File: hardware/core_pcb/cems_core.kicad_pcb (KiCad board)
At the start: 4 copper layers, 211.5 x 85.1 mm, 423 parts, among them J1 24VDC IN, J10 BANK A IDC26, J11 BANK B, J12 INPUTS IDC26, J13 FIELD A 24V, J14 FIELD B 24V, J15 PUMP POWER, J16 PUMP SIGNALS, J17 RELAY COILS, J18 USB-C, J19 TEMP1, J2 CLIENT, J20 TEMP2, J21 TEMP3, J22 AI 1-2, J23 AI 3-4, J24 AI 5-6, J25 SENSORS, J3 I/O ONLY, J4 RVT70 RiBUS, J5 SWD, J6 SERVICE UART, J7 ROLE, Q1 2N7002, Q2 BC817, Q3 BC807, Q4 2N7002, Q5 BC817, Q6 BC807, SW1 RESET, U1 TPS54360B, U10 APS6404L, U11 MAX6369, U12 74LVC1G08, U13 74LVC1G04, U14 ISO2H823V2.5, U15 ISO808A-1, U16 ISO1I813T, U17 L78L05, U18 ISO7741, U19 74LVC1G08, U2 TLV62569DBV, U20 74LVC1G08, U21 IPS7091S, U22 74LVC1G14, U23 74LVC1G14, U24 LMV331, U25 CPC1017N, U26 CPC1017N, U27 USBLC6-2SC6, U28 ISOW7741, U29 74LVC1G04, U3 STM32H573VIT6, U30 ADS124S08, U31 ISOW7741, U32 74LVC1G04, U33 ITX2424SA, U34 AD4112, U35 L78L05, U36 LM317L, U37 REF5010, U38 LT3045, U4 LAN8742A-CZ, U5 TPD4E05U06, U6 W5500, U7 TPD4E05U06, U8 W25Q128JV, U9 MB85RC1MT, Y1 25MHz, Y2 32.768kHz, Y3 25MHz, Y4 25MHz

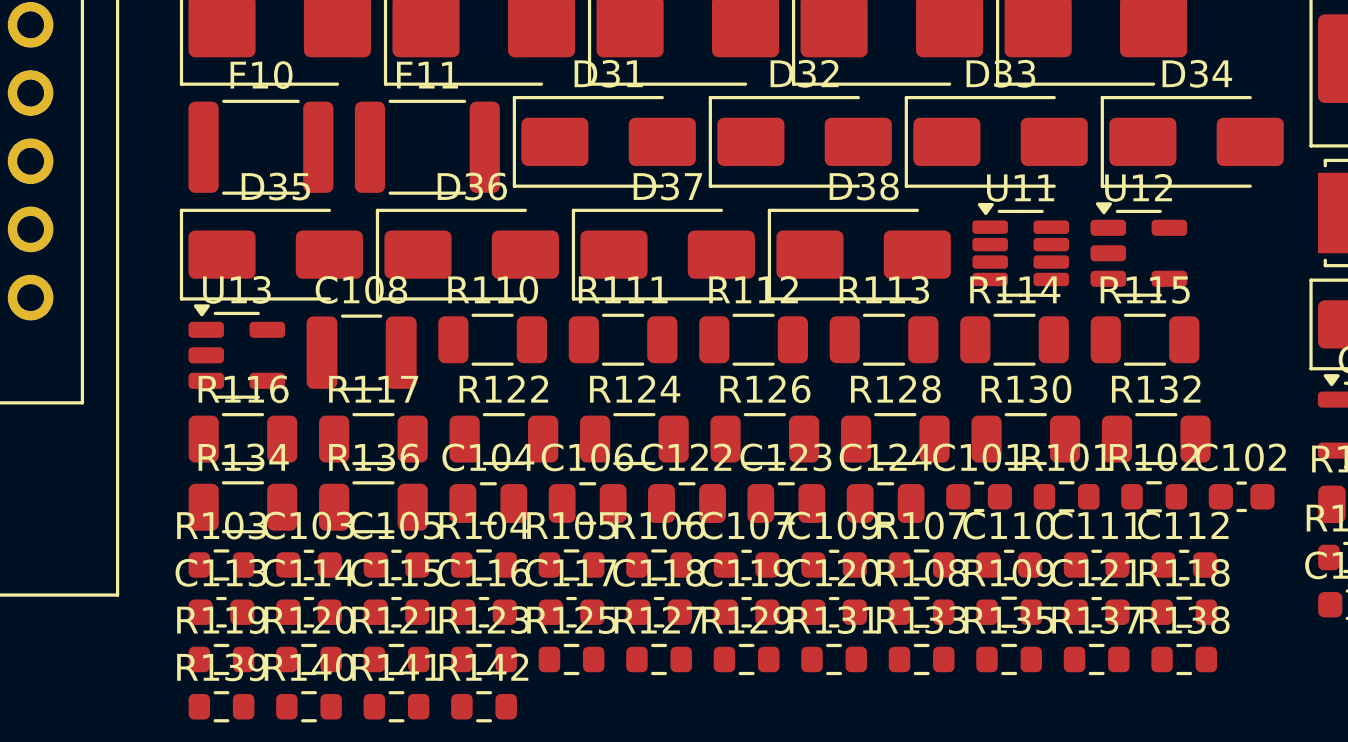
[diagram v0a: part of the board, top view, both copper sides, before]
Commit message: CORE PCB: I/O chip pinouts checked against datasheets; gate latch, ODIS polarity
Pin tables of AD4112, ADS124S08, ISO2H823V2.5, ISO1I813T, ISO808A-1, ISO7741 and
ISOW7741 compared with the datasheets: all match. Fixes from the check: ISO2H823 /ODIS
is active low (takes GATE directly); OLADJ fitted 12.1k; CLKADJ 10k 0.1 %; ROSC 22.1k;
ISOW7741 EN/FLT pulled to 3.3 V; MAX6369 WDO only pulses, so a 74LVC1G175 latches a
trip until GATE_EN is re-armed. hardware/datasheets/IO_CHIPS_DATASHEET_CHECK.md holds the
extracts and the AD4112 register facts for the driver.

Co-Authored-By: Claude Opus 5.5 <noreply@anthropic.com>
Claude-Session: https://claude.ai/code/session_014onnq3eRiDkqdAB6fKiRDW
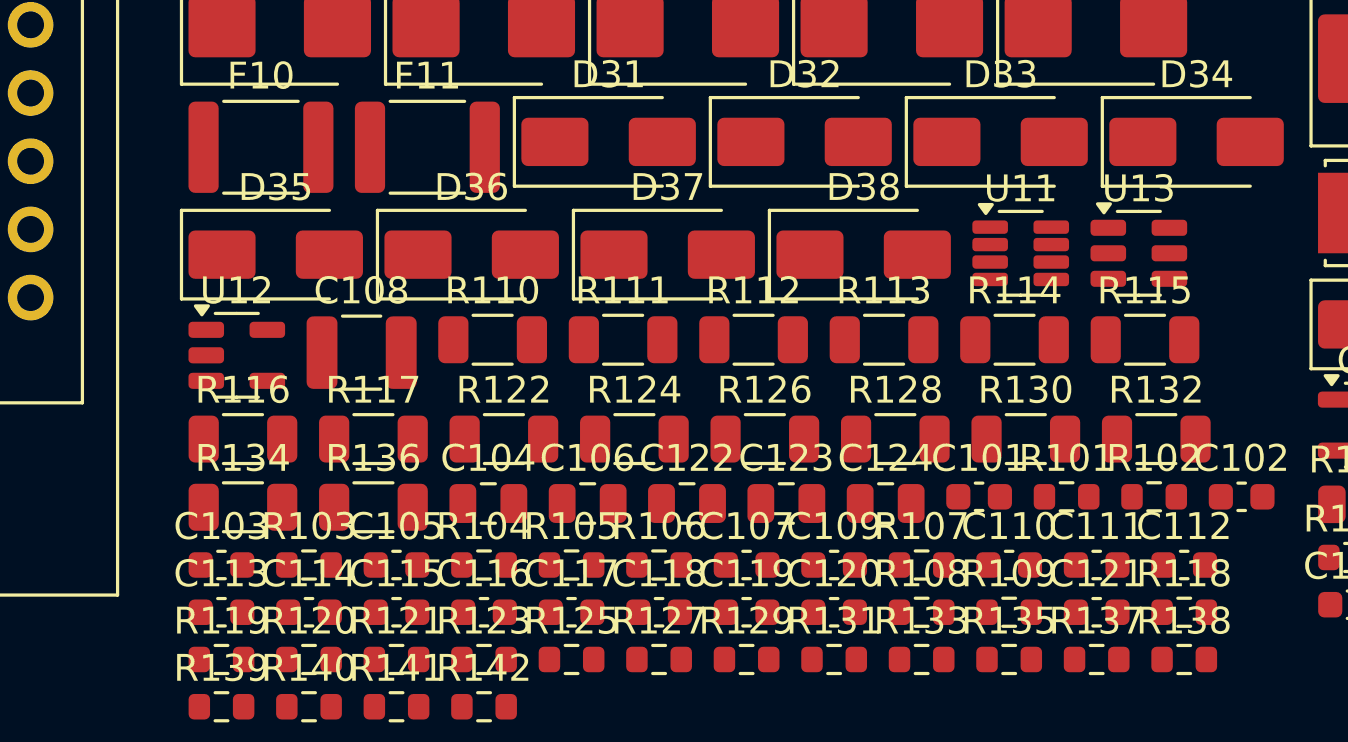
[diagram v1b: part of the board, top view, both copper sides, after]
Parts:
- R104: value 10k -> 10k 0.1%
- R106: value DNF -> 12k1 1%
- R118: value 22k 1% -> 22k1 1%
- U13: value 74LVC1G04 -> 74LVC1G175; footprint Package_TO_SOT_SMD:SOT-23-5 -> Package_TO_SOT_SMD:SOT-23-6
- moved U12 33.8 mm to (198.0, 156.1)
- moved U13 33.8 mm to (231.6, 152.3)
- moved C103 3.26 mm to (197.4, 163.9)
- moved R103 3.26 mm to (200.7, 163.9)
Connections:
- R164 pad 1: +5V -> +3V3
- R176 pad 1: +5V -> +3V3
- U12 pad 2: WDO_N -> GATE_ARM
- U13 pad 1: (no net) -> GATE_EN
- U13 pad 2: GATE -> GND
- U13 pad 3: GND -> +3V3
- U13 pad 4: GATE_N -> GATE_ARM
- U14 pad 40: GATE_N -> GATE

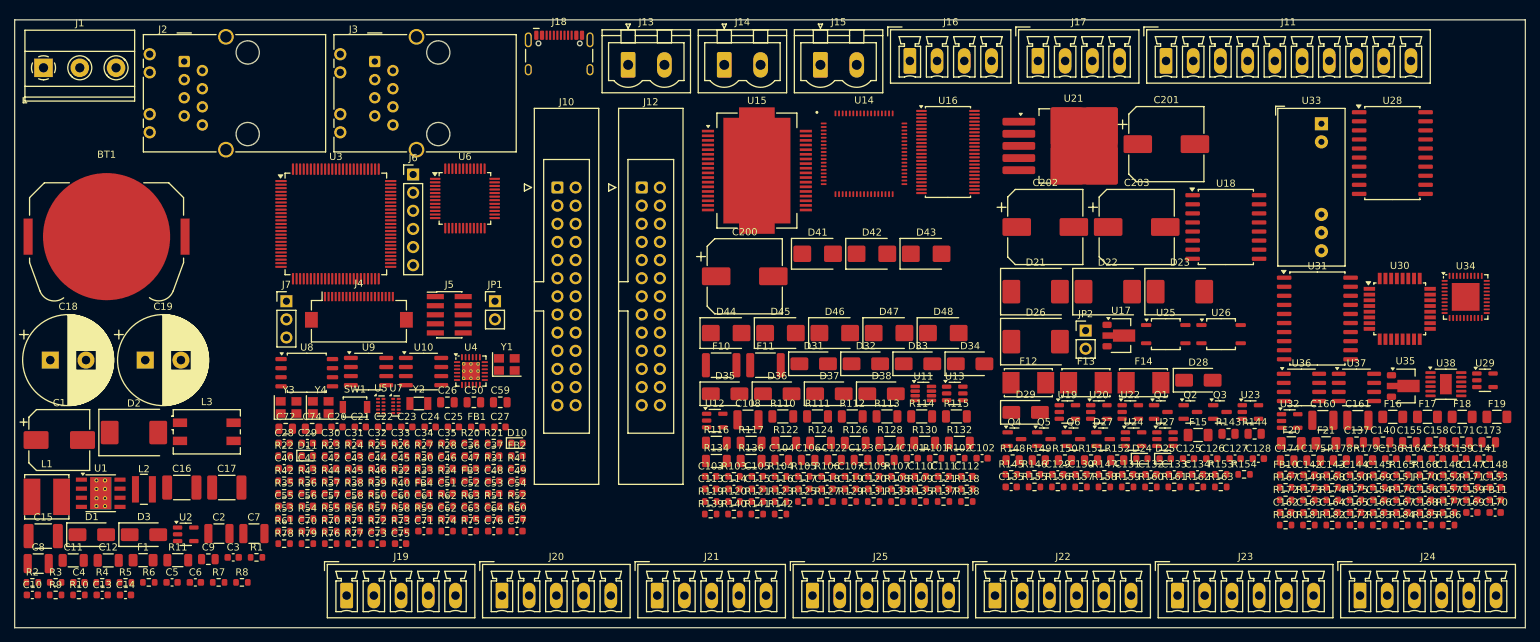
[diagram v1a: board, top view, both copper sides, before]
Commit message: One 40-way ribbon for all digital I/O (Gary, 31 Oct)
Main board: J10 becomes a 40-way latched IDC header carrying bank A outputs 1-8 (pins
1-16, each beside its 0 V) and inputs 1-8 (pins 17-32), with 4 x +24 V and 4 x 0 V; J12
and F11 removed, so no ribbon can go into the wrong slot. Breakout rev 0.2: one board,
50 x 80 mm, two-tier 3.81 mm pluggable headers (valves OUT over 0V, inputs IN over +24V,
plus a 0V strip for 3-wire sensors), LEDs on every channel, flyback options on the valves.
Two-tier footprint is a placeholder until the maker's drawing is checked.

Co-Authored-By: Claude Opus 5.5 <noreply@anthropic.com>
Claude-Session: https://claude.ai/code/session_014onnq3eRiDkqdAB6fKiRDW
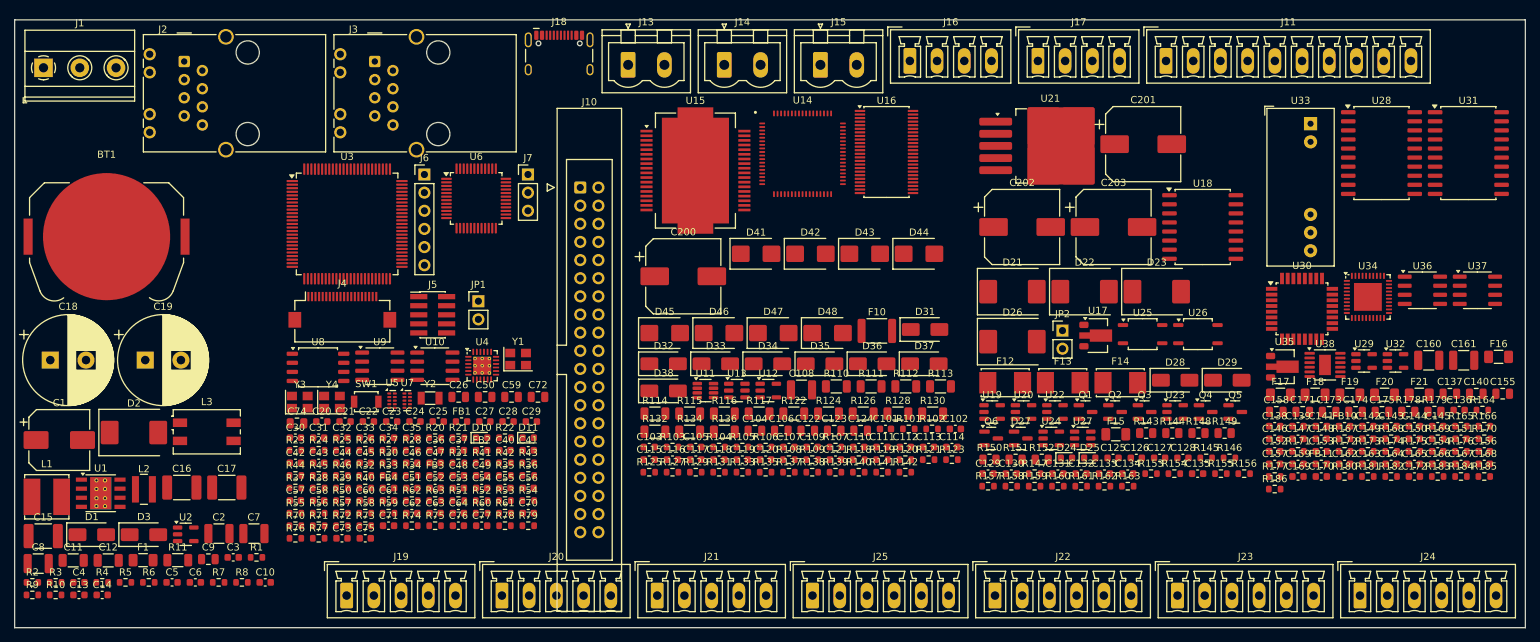
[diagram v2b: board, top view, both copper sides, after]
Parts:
- removed F11: 0.75A, Fuse:Fuse_1812_4532Metric
- removed J12: INPUTS IDC26, Connector_IDC:IDC-Header_2x13_P2.54mm_Latch_Vertical
- J10: value BANK A IDC26 -> DIGITAL I/O IDC40; footprint Connector_IDC:IDC-Header_2x13_P2.54mm_Latch_Vertical -> Connector_IDC:IDC-Header_2x20_P2.54mm_Latch_Vertical
- moved R132 42.7 mm to (189.6, 157.7)
- moved J7 38.2 mm to (171.9, 121.6)
- moved R114 37.3 mm to (189.6, 155.1)
- moved R115 37.3 mm to (194.5, 155.1)
- moved C72 35.6 mm to (173.3, 152.8)
- moved C10 32.6 mm to (135.1, 178.8)
- moved C28 31.5 mm to (169.1, 156.2)
- moved C29 31.5 mm to (172.3, 156.2)
- moved U31 31.4 mm to (303.5, 118.6)
- moved C113 31.1 mm to (228.0, 159.8)
- moved C114 31.1 mm to (231.2, 159.8)
- moved R78 31.0 mm to (168.6, 170.8)
- moved R79 31.0 mm to (171.9, 170.8)
- moved C40 31.0 mm to (168.6, 160.3)
- moved C41 31.0 mm to (171.9, 160.3)
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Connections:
- F10 pad 2: +24V_RA -> +24V_RIB
- J10 pad 17: +24V_RA -> DI1
- J10 pad 19: +24V_RA -> DI2
- J10 pad 21: +24V_RA -> DI3
- J10 pad 23: +24V_RA -> DI4
- J10 pad 25: +24V_RA -> DI5

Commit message: CORE PCB + breakout: make every user plug fit only its own header
Three pitch families (5.08 power/24 V outputs, 3.81 bank B, 3.5 sensors), one size per
header except the harmless temperature and 4-20 mA groups, and a coding key per header
(script-checked against every plug and shift). J13+J14 merged into one 4-way field plug;
pump power and signals on one 6-way plug (J16 gone); relays 3-way. Survival layer: 1k 1 W
pump outputs, per-channel relay PTCs + CPC1014N, 30 mA loop current limiters, TVS on the
5 V and 10 V sensor supplies. CORE_PCB.md section 15 has the mis-plug tables.

Co-Authored-By: Claude Opus 5.5 <noreply@anthropic.com>
Claude-Session: https://claude.ai/code/session_014onnq3eRiDkqdAB6fKiRDW
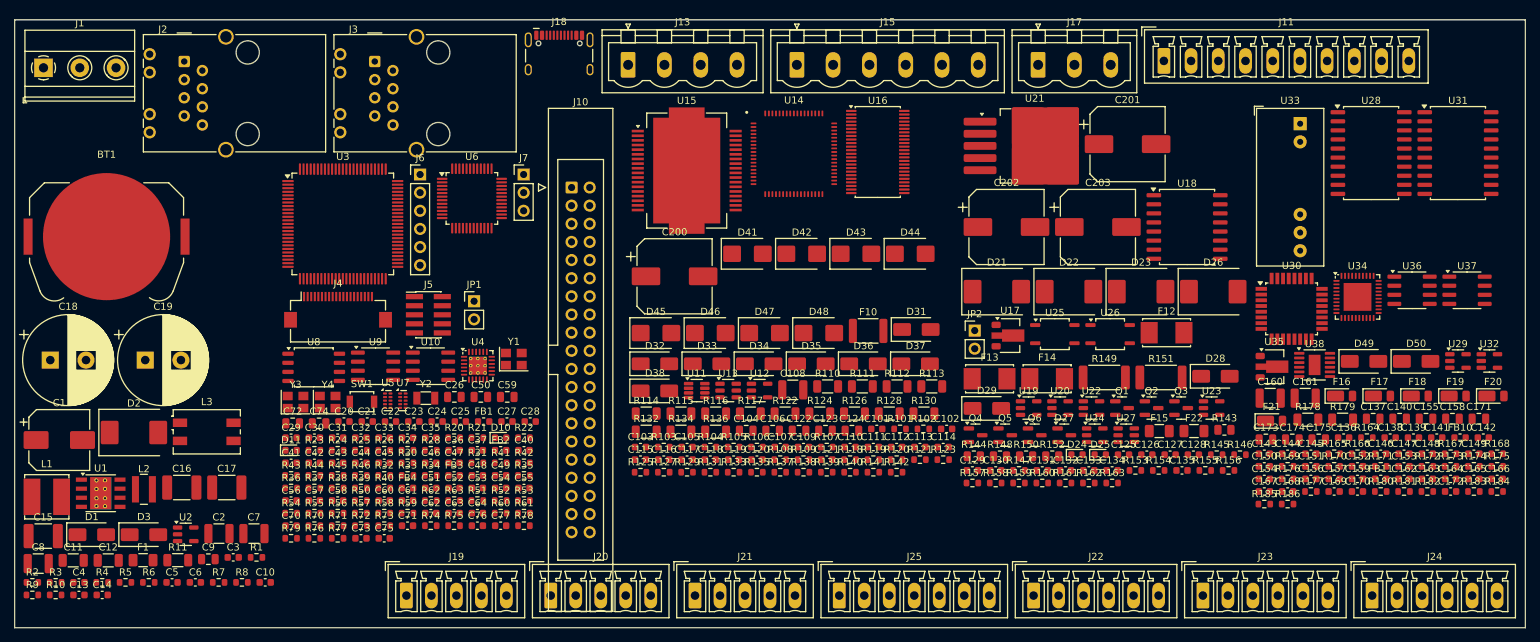
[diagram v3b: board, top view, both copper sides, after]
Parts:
- removed J14: FIELD B 24V, Connector_Phoenix_MSTB:PhoenixContact_MSTBVA_2,5_2-G-5,08_1x02_P5.08mm_Vertical
- removed J16: PUMP SIGNALS, Connector_Phoenix_MC:PhoenixContact_MCV_1,5_4-G-3.81_1x04_P3.81mm_Vertical
- added D49: SMAJ5.0A, Diode_SMD:D_SMA, F.Cu at (288.9, 147.8)
- added D50: SMAJ11A, Diode_SMD:D_SMA, F.Cu at (296.2, 147.8)
- added F22: 50mA, Fuse:Fuse_1206_3216Metric, F.Cu at (265.1, 157.6)
- F15: value 0.2A -> 50mA
- F16, F17, F18, F19, F20, F21: value 50mA -> CCR 30mA; footprint Fuse:Fuse_1206_3216Metric -> Diode_SMD:D_PowerDI-123
- J13: value FIELD A 24V -> FIELD 24V A+B; footprint Connector_Phoenix_MSTB:PhoenixContact_MSTBVA_2,5_2-G-5,08_1x02_P5.08mm_Vertical -> Connector_Phoenix_MSTB:PhoenixContact_MSTBVA_2,5_4-G-5,08_1x04_P5.08mm_Vertical
- J15: value PUMP POWER -> PUMP; footprint Connector_Phoenix_MSTB:PhoenixContact_MSTBVA_2,5_2-G-5,08_1x02_P5.08mm_Vertical -> Connector_Phoenix_MSTB:PhoenixContact_MSTBVA_2,5_6-G-5,08_1x06_P5.08mm_Vertical
- J17: footprint Connector_Phoenix_MC:PhoenixContact_MCV_1,5_4-G-3.81_1x04_P3.81mm_Vertical -> Connector_Phoenix_MSTB:PhoenixContact_MSTBVA_2,5_3-G-5,08_1x03_P5.08mm_Vertical
- J19, J20, J21: footprint Connector_Phoenix_MC:PhoenixContact_MCV_1,5_5-G-3.81_1x05_P3.81mm_Vertical -> Connector_Phoenix_MC:PhoenixContact_MCV_1,5_5-G-3.5_1x05_P3.50mm_Vertical
- J22, J23, J24: footprint Connector_Phoenix_MC:PhoenixContact_MCV_1,5_6-G-3.81_1x06_P3.81mm_Vertical -> Connector_Phoenix_MC:PhoenixContact_MCV_1,5_6-G-3.5_1x06_P3.50mm_Vertical
- J25: footprint Connector_Phoenix_MC:PhoenixContact_MCV_1,5_6-G-3.81_1x06_P3.81mm_Vertical -> Connector_Phoenix_MC:PhoenixContact_MCV_1,5_7-G-3.5_1x07_P3.50mm_Vertical
- R149, R151: value 47R -> 1k 1W; footprint Resistor_SMD:R_0805_2012Metric -> Resistor_SMD:R_2512_6332Metric
- R178, R179: footprint Resistor_SMD:R_0805_2012Metric -> Resistor_SMD:R_1206_3216Metric
- moved C72 34.5 mm to (138.9, 156.5)
- moved D29 33.9 mm to (236.1, 154.4)
- moved C29 33.7 mm to (138.7, 158.5)
- moved C41 33.2 mm to (138.7, 162.0)
- moved C56 33.2 mm to (138.7, 167.3)
- moved D11 33.2 mm to (138.7, 160.3)
- moved R36 33.2 mm to (138.7, 165.5)
- moved R43 33.2 mm to (138.7, 163.8)
- moved R54 33.2 mm to (138.7, 169.1)
- moved R79 33.2 mm to (138.7, 172.6)
- moved C70 33.2 mm to (138.7, 170.8)
- moved Q5 32.4 mm to (238.7, 158.1)
- moved Q4 32.4 mm to (234.5, 158.1)
- moved R185 31.0 mm to (275.0, 167.8)
- moved D26 29.0 mm to (267.8, 138.0)
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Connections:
- F15 pad 2: +24V_REL -> +24V_REL1
- F16 pad 1: +24V_AI -> LOOP1
- F16 pad 2: LOOP1 -> +24V_AI
- F17 pad 1: +24V_AI -> LOOP2
- F17 pad 2: LOOP2 -> +24V_AI
- F18 pad 1: +24V_AI -> LOOP3
- F18 pad 2: LOOP3 -> +24V_AI
- F19 pad 1: +24V_AI -> LOOP4
- F19 pad 2: LOOP4 -> +24V_AI
- F20 pad 1: +24V_AI -> LOOP5
- F20 pad 2: LOOP5 -> +24V_AI
- F21 pad 1: +24V_AI -> LOOP6
- F21 pad 2: LOOP6 -> +24V_AI
- J17 pad 2: FIELD_0V -> REL2_OUT
- J17 pad 3: REL2_OUT -> FIELD_0V
- U25 pad 3: +24V_REL -> +24V_REL1
- U26 pad 3: +24V_REL -> +24V_REL2
